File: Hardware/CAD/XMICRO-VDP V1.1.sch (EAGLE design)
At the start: 87 parts, among them J1 PJRAN1XU04AUX, J2 MINI-DIN4, J4 PINHD-2X6, J5 PINHD-1X8, Q1 VN2106, Q2 VN2106, U1 74574, U10 7414, U11 7404, U12 74244, U13 7432, U14 74574, U15 74244, U16 74245, U17 V9958, U18 CXA2075, U2 AS6C4008, U3 74574, U4 74574, U5 7404, U6 7410, U7 74138, U8 74373, U9 7474, Y1 5MHz, Y2 21.47727MHz

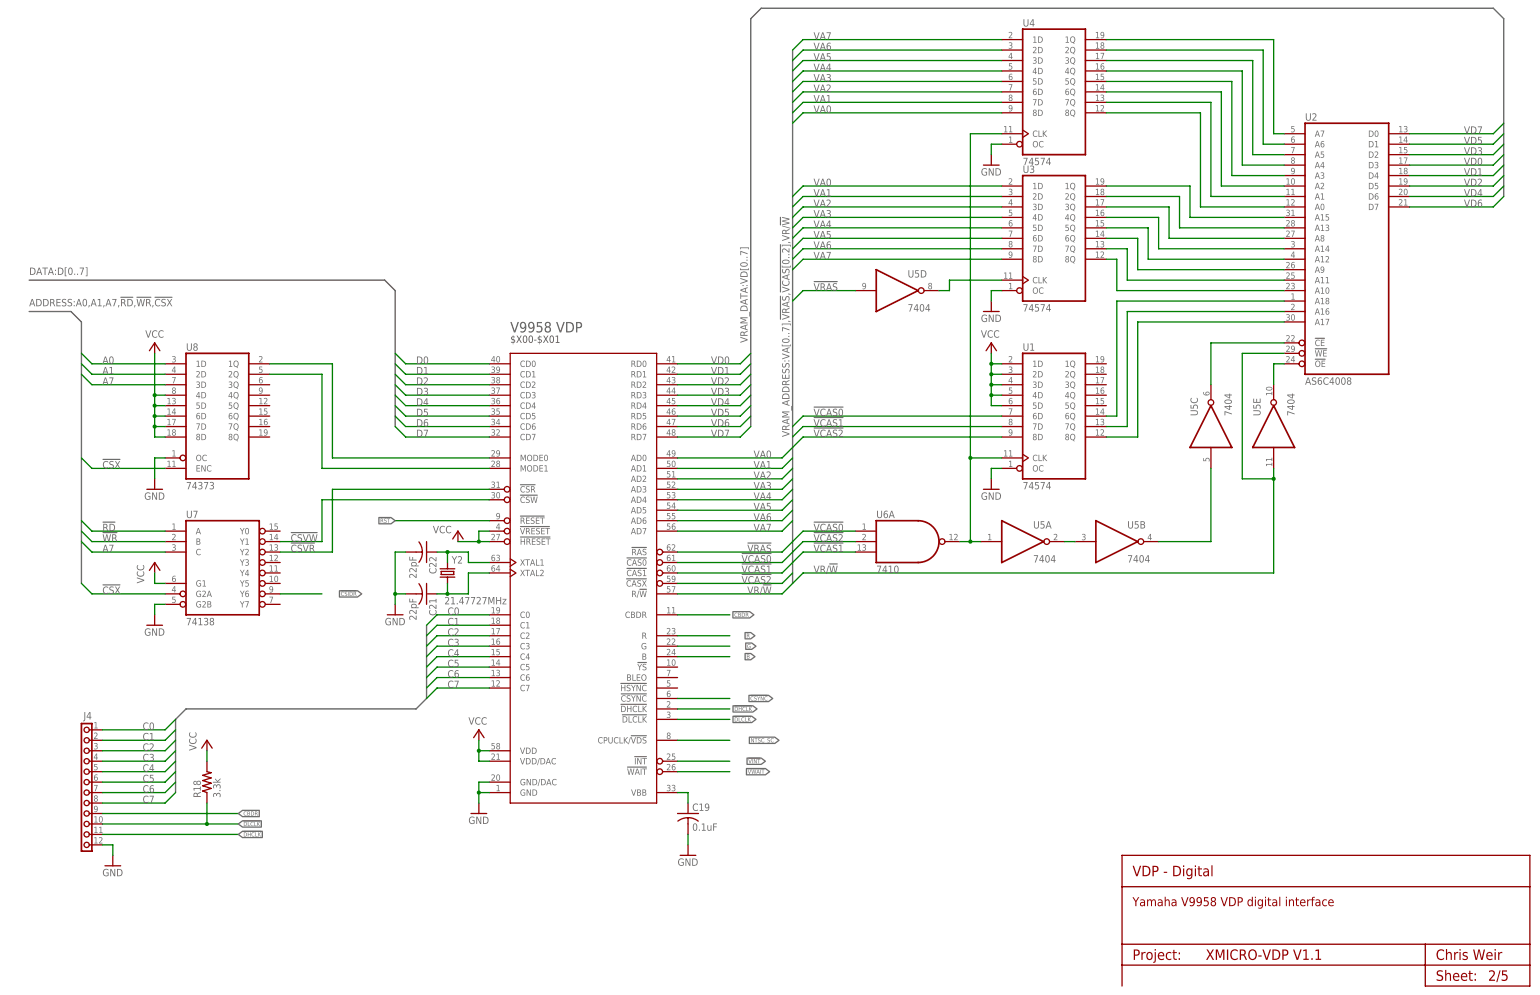
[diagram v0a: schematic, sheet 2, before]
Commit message: Updated to XMICRO-VDP V1.1. Replaced VRAM with dynamic RAM, various other minor tweaks.
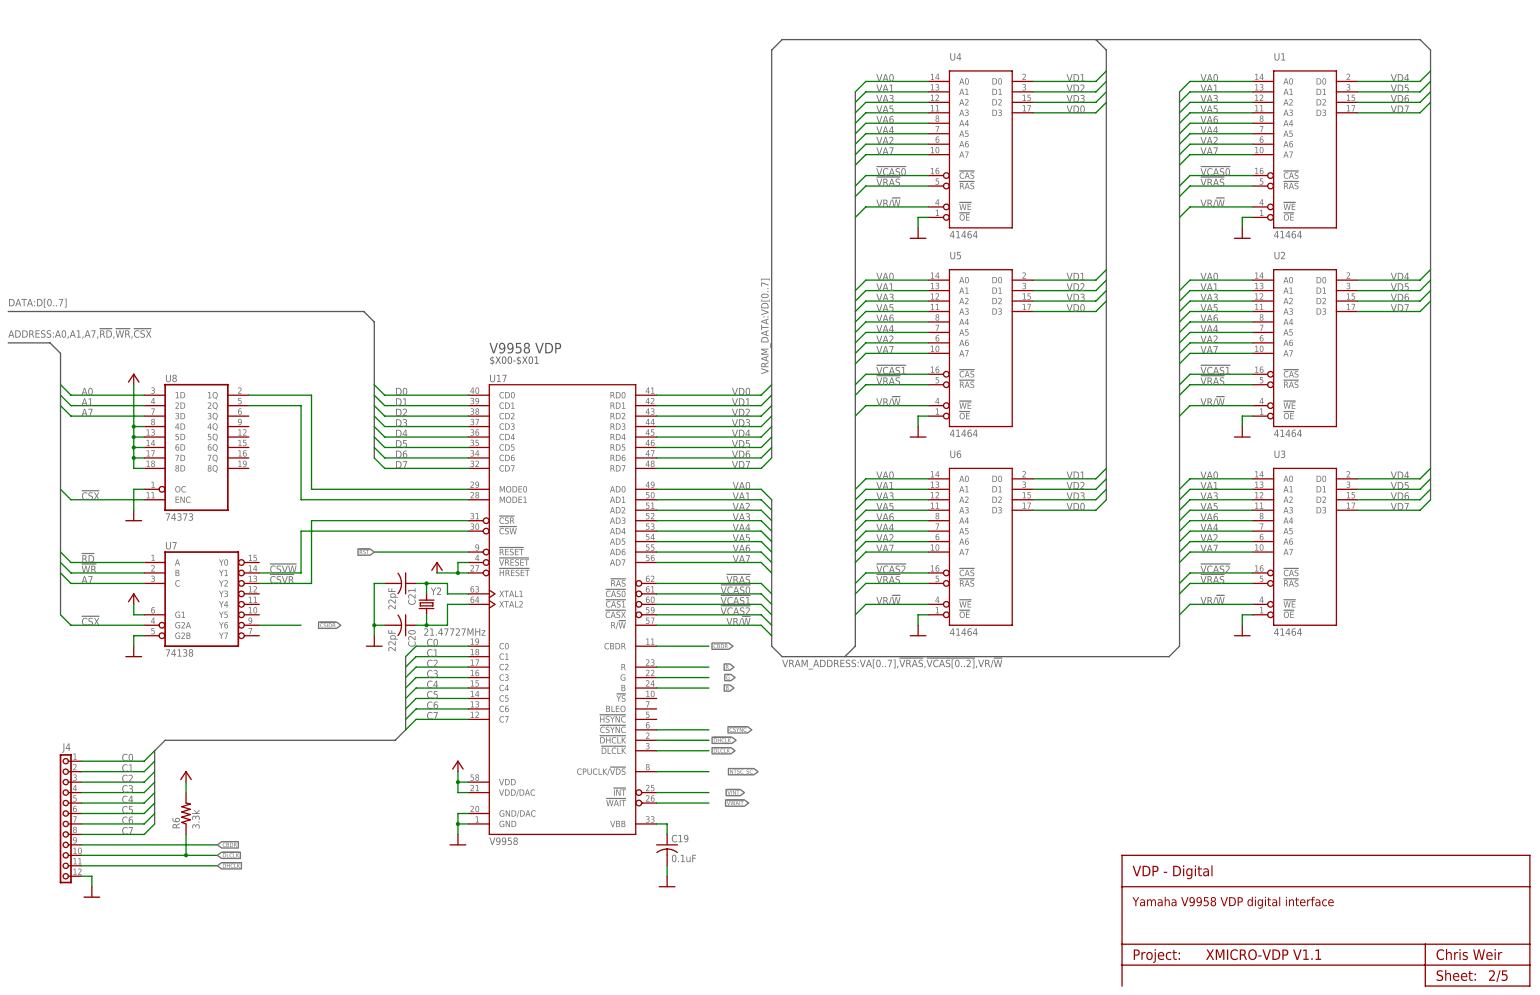
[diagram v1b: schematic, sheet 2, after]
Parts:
- added C38, C39: 220uF, rcl:CPOL-USE2.5-7
- added J3: PINHD1X3, Custom:PINHD1X3
- added R19: 240, rcl:R-US_0207/10
- C20: value 47uF -> 22pF; device rcl:CPOL-USE2.5-6 -> Custom:C-US100
- C22: value 22pF -> 0.1uF
- C24: value 220uF -> 0.1uF; device Custom:CPOL-US-10-5 -> Custom:C-US100
- C26: value 0.1uF -> 5pF
- C27: value 0.1uF -> 47pF
- C28: value 5pF -> 10nF
- C29: value 47pF -> 10nF; device Custom:C-US100 -> rcl:C-US050-024X044
- C30: value 10nF -> 28pF
- C31: value 10nF -> 47uF; device Custom:C-US100 -> rcl:CPOL-USE2.5-6
- C34: value 28pF -> 470uF; device Custom:C-US100 -> Custom:CPOL-US-10-5
- C35, C36: value 220uF -> 47uF
- C37: device rcl:CPOL-USE2.5-6 -> rcl:CPOL-USE2.5-7
- L1: device rcl:L-US0204V -> rcl:L-US0207/10
- R1, RN1: value 10k -> 3.3k
- R10: value 2.2k -> 0
- R11: value 0 -> 2.2k
- R13: value 3.32k/1% -> 0
- R14: value 75 -> 2.2k
- R15: value 75 -> 3.32k/1%
- R16: value 43 -> 75
- R17: value 240 -> 75
- R18: value 3.3k -> 43
- R2: value 3.3k -> 10k
- R3: value 0 -> 3.3k
- R5: value 470 -> 0
- R6: value 470 -> 3.3k
- R8: value 0 -> 470
- R9: value 2.2k -> 470
- U1, U3, U4: value 74574 -> 41464; device 74xx-us:74HC574N -> Custom:41464
- U2: value AS6C4008 -> 41464; device Custom:4008-VDP -> Custom:41464
- U5: value 7404 -> 41464; device 74xx-us:74LS04N -> Custom:41464
- U6: value 7410 -> 41464; device 74xx-us:74LS10N -> Custom:41464
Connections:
- removed net N$31: U3A.CLK, U5D.O
- removed net N$32: U2G$1.A0, U4A.8Q
- removed net N$41: U2G$1.A1, U4A.7Q
- removed net N$42: U2G$1.A2, U4A.6Q
- removed net N$43: U2G$1.A3, U4A.5Q
- removed net N$44: U2G$1.A4, U4A.4Q
- removed net N$45: U2G$1.A5, U4A.3Q
- removed net N$46: U2G$1.A6, U4A.2Q
- removed net N$47: U2G$1.A7, U4A.1Q
- removed net N$48: U1A.CLK, U4A.CLK, U5A.I, U6A.O
- removed net N$49: U2G$1.!OE, U5E.O
- removed net N$50: U2G$1.!CE, U5C.O
- removed net N$57: U2G$1.A10, U3A.8Q
- removed net N$58: U2G$1.A11, U3A.7Q
- removed net N$59: U2G$1.A9, U3A.6Q
- removed net N$60: U2G$1.A12, U3A.5Q
- removed net N$61: U2G$1.A14, U3A.4Q
- removed net N$62: U2G$1.A8, U3A.3Q
- removed net N$63: U2G$1.A13, U3A.2Q
- removed net N$64: U2G$1.A15, U3A.1Q
- removed net N$65: U1A.7Q, U2G$1.A16
- removed net N$66: U1A.8Q, U2G$1.A17
- removed net N$67: U1A.6Q, U2G$1.A18
- removed net N$76: U5A.O, U5B.I
- removed net N$78: U11D.O, U6B.I1
- removed net N$80: U5B.O, U5C.I
- new net N$1: U13A.I1, U9B.Q
- new net N$2: J3.3, U18.BOUT@21
- new net N$6: J3.2, U18.GOUT@22
- new net N$7: J3.1, U18.ROUT@23
- net !CSYNC: now also R14.1; no longer R12.1
- net !DLCLK: now also R6.1; no longer R18.1
- net !VCAS0: now also U1G$1.!CAS, U4G$1.!CAS; no longer U1A.6D, U6A.I0
- net !VCAS1: now also U2G$1.!CAS, U5G$1.!CAS; no longer U1A.7D, U6A.I2
- net !VCAS2: now also U3G$1.!CAS, U6G$1.!CAS; no longer U1A.8D, U6A.I1
- net !VINT: now also R1.1
- net !VRAS: now also U1G$1.!RAS, U2G$1.!RAS, U3G$1.!RAS, U4G$1.!RAS, U5G$1.!RAS, U6G$1.!RAS; no longer U5D.I
- net !VWAIT: now also R3.1; no longer R2.1
- net B: now also C25.1, R9.2; no longer C27.1, R7.2
- net G: now also C24.1, R8.2; no longer C26.1, R6.2
- net GND: now also C20.2, C26.2, C27.2, C31.-, C34.-, C35.-, C36.-, R13.2, R19.1, R8.1, R9.1, U1G$1.!OE, U2G$1.!OE, U3G$1.!OE, U4G$1.!OE, U5G$1.!OE, U6G$1.!OE; no longer C20.-, C23.2, C24.-, C30.2, C31.2, R11.2, R17.1, R5.1, R6.1, U1A.OC, U3A.OC, U4A.OC
- net N$11: now also R5.1; no longer R4.1
- net N$12: now also R17.1; no longer R15.1
- net N$13: now also R16.1; no longer R14.1
- net N$14: now also R18.1; no longer R16.1
- net N$15: now also C39.+, R18.2, R19.2; no longer C37.+, R16.2, R17.2
- net N$16: now also C37.+, R16.2; no longer C35.+, R14.2
- net N$17: now also C38.+, R17.2; no longer C36.+, R15.2
- net N$19: now also U11D.O; no longer U10B.O
- net N$20: now also U11D.I; no longer U10B.I
- net N$21: now also C30.2; no longer C34.2
- net N$22: now also C27.1, R14.2; no longer C29.1, R12.2
- net N$26: now also R10.1, R13.1; no longer R11.1, R8.1
- net N$28: now also C21.1; no longer C22.1
- net N$29: now also C38.-; no longer C36.-
- net N$3: now also C23.2; no longer C25.2
- net N$30: now also C20.1; no longer C21.1
- net N$4: now also C24.2; no longer C26.2
- net N$5: now also C25.2; no longer C27.2
- net N$51: now also R4.2; no longer R3.2
- net N$53: now also C39.-; no longer C37.-
- net N$71: now also C30.1, R15.2; no longer C34.1, R13.2
- net N$73: now also R4.1, U13A.O; no longer R3.1, U6B.O
- net N$77: now also U13A.I0; no longer U11D.I
- net N$79: no longer U6B.I2
- net N$81: now also C37.-; no longer C35.-
- net N$83: now also R2.1; no longer R1.1
- net N$9: now also R5.2; no longer R4.2
- net NTSC_SC: now also R11.1; no longer R9.1
- net PAL_SC: now also R12.1; no longer R10.1
- net R: now also C23.1, R7.2; no longer C25.1, R5.2
- net SC: now also C26.1, R11.2, R12.2; no longer C28.1, R10.2, R9.2
- net VA0: now also U1G$1.A0, U2G$1.A0, U3G$1.A0, U4G$1.A0, U5G$1.A0, U6G$1.A0; no longer U3A.1D, U4A.8D
- net VA1: now also U1G$1.A1, U2G$1.A1, U3G$1.A1, U4G$1.A1, U5G$1.A1, U6G$1.A1; no longer U3A.2D, U4A.7D
- net VA2: now also U1G$1.A6, U2G$1.A6, U3G$1.A6, U4G$1.A6, U5G$1.A6, U6G$1.A6; no longer U3A.3D, U4A.6D
- net VA3: now also U1G$1.A2, U2G$1.A2, U3G$1.A2, U4G$1.A2, U5G$1.A2, U6G$1.A2; no longer U3A.4D, U4A.5D
- net VA4: now also U1G$1.A5, U2G$1.A5, U3G$1.A5, U4G$1.A5, U5G$1.A5, U6G$1.A5; no longer U3A.5D, U4A.4D
- net VA5: now also U1G$1.A3, U2G$1.A3, U3G$1.A3, U4G$1.A3, U5G$1.A3, U6G$1.A3; no longer U3A.6D, U4A.3D
- net VA6: now also U1G$1.A4, U2G$1.A4, U3G$1.A4, U4G$1.A4, U5G$1.A4, U6G$1.A4; no longer U3A.7D, U4A.2D
- net VA7: now also U1G$1.A7, U2G$1.A7, U3G$1.A7, U4G$1.A7, U5G$1.A7, U6G$1.A7; no longer U3A.8D, U4A.1D
- net VCC: now also C22.1, C28.1, C29.1, C31.+, C34.+, C35.+, C36.+, R10.2, R15.1, R3.2, R6.2, U10B.I; no longer C20.+, C23.1, C24.+, C30.1, C31.1, R13.1, R18.2, R8.2, U13A.I0, U13A.I1, U1A.1D, U1A.2D, U1A.3D, U1A.4D, U1A.5D, U5F.I, U6B.I0, U6C.I0, U6C.I1, U6C.I2
- net VD0: now also U4G$1.D3, U5G$1.D3, U6G$1.D3; no longer U2G$1.D3
- net VD1: now also U4G$1.D0, U5G$1.D0, U6G$1.D0; no longer U2G$1.D4
- net VD2: now also U4G$1.D1, U5G$1.D1, U6G$1.D1; no longer U2G$1.D5
- net VD3: now also U4G$1.D2, U5G$1.D2, U6G$1.D2; no longer U2G$1.D2
- net VD4: now also U1G$1.D0, U2G$1.D0, U3G$1.D0; no longer U2G$1.D6
- net VD5: now also U1G$1.D1, U3G$1.D1
- net VD6: now also U1G$1.D2, U2G$1.D2, U3G$1.D2; no longer U2G$1.D7
- net VD7: now also U1G$1.D3, U2G$1.D3, U3G$1.D3; no longer U2G$1.D0
- net VR/!W: now also U1G$1.!WE, U3G$1.!WE, U4G$1.!WE, U5G$1.!WE, U6G$1.!WE; no longer U5E.I
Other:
- note added: "B"
- note added: "CXA2075 Bypassing"
- note added: "G"
- note added: "General Bypassing"
- note added: "Local Storage"
- note added: "Luma Trap: Populate R13 OR C34 + L1 See CXA2075 datasheet for appropriate values."
- note added: "R"
- note removed: "Luma Trap: Populate R13 OR C34 & L1 See CXA2075 datasheet for values."
- moved on the sheet: C1, C10, C11, C12, C13, C14, C15, C16, C17, C18, C19, C2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
